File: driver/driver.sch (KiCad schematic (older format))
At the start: 102 parts, among them J1 OUT_A, J10 FAN, J2 OUT_B, J3 UART_DEBUG, J4 USB_B_Micro, J5 CH340E module, J6 1602 I2C LCD, J7 IN_VCC, J8 IN_GND, J9 SWD, Q1 TPHR6503PL, Q2 TPHR6503PL, Q3 TPHR6503PL, Q4 TPHR6503PL, SW2 SW_Push, U1 MT3608, U10 PC817, U2 AMS1117-5.0, U3 AMS1117-3.3, U4 TC4427, U5 TC4427, U6 STM32F103C8Tx, U7 INA226, U8 MCP9804_MSOP, U9 PC817, Y1 8MHz

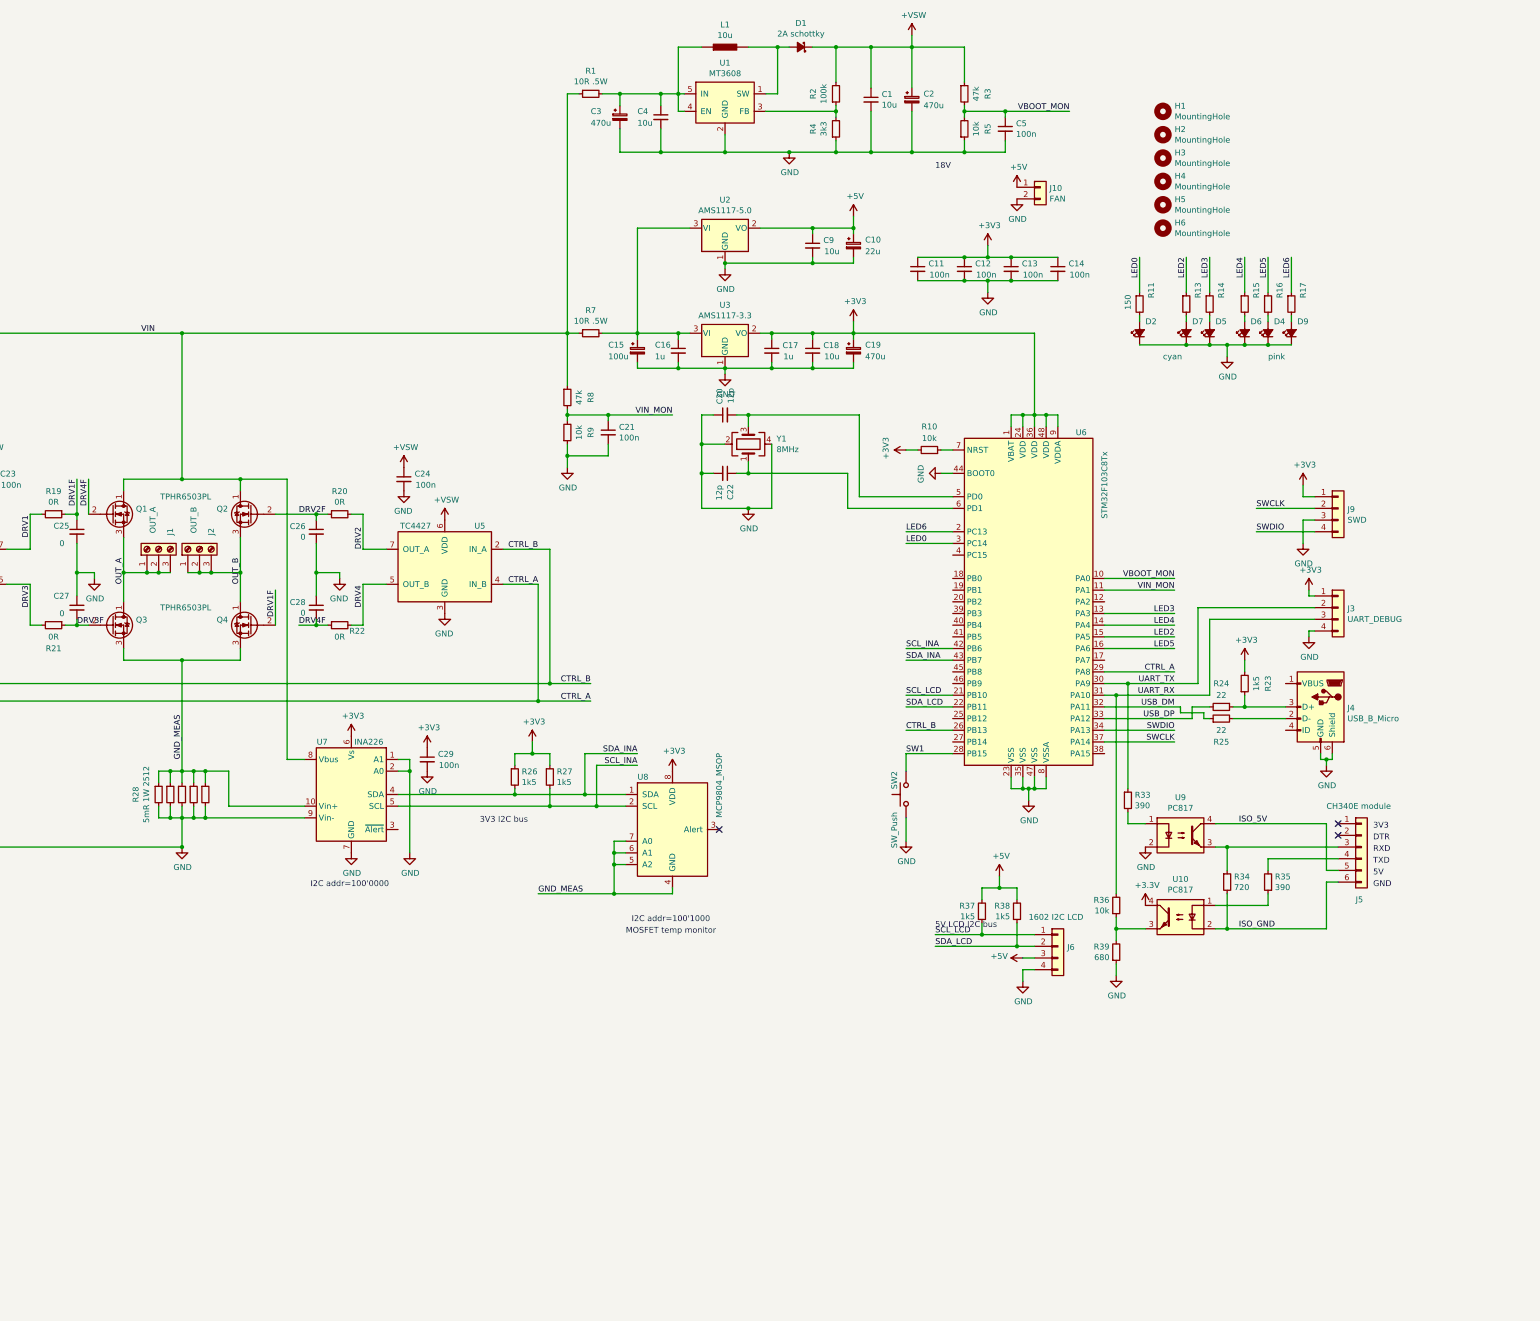
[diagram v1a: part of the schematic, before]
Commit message: Throw out a bunch, use a different microcontroller
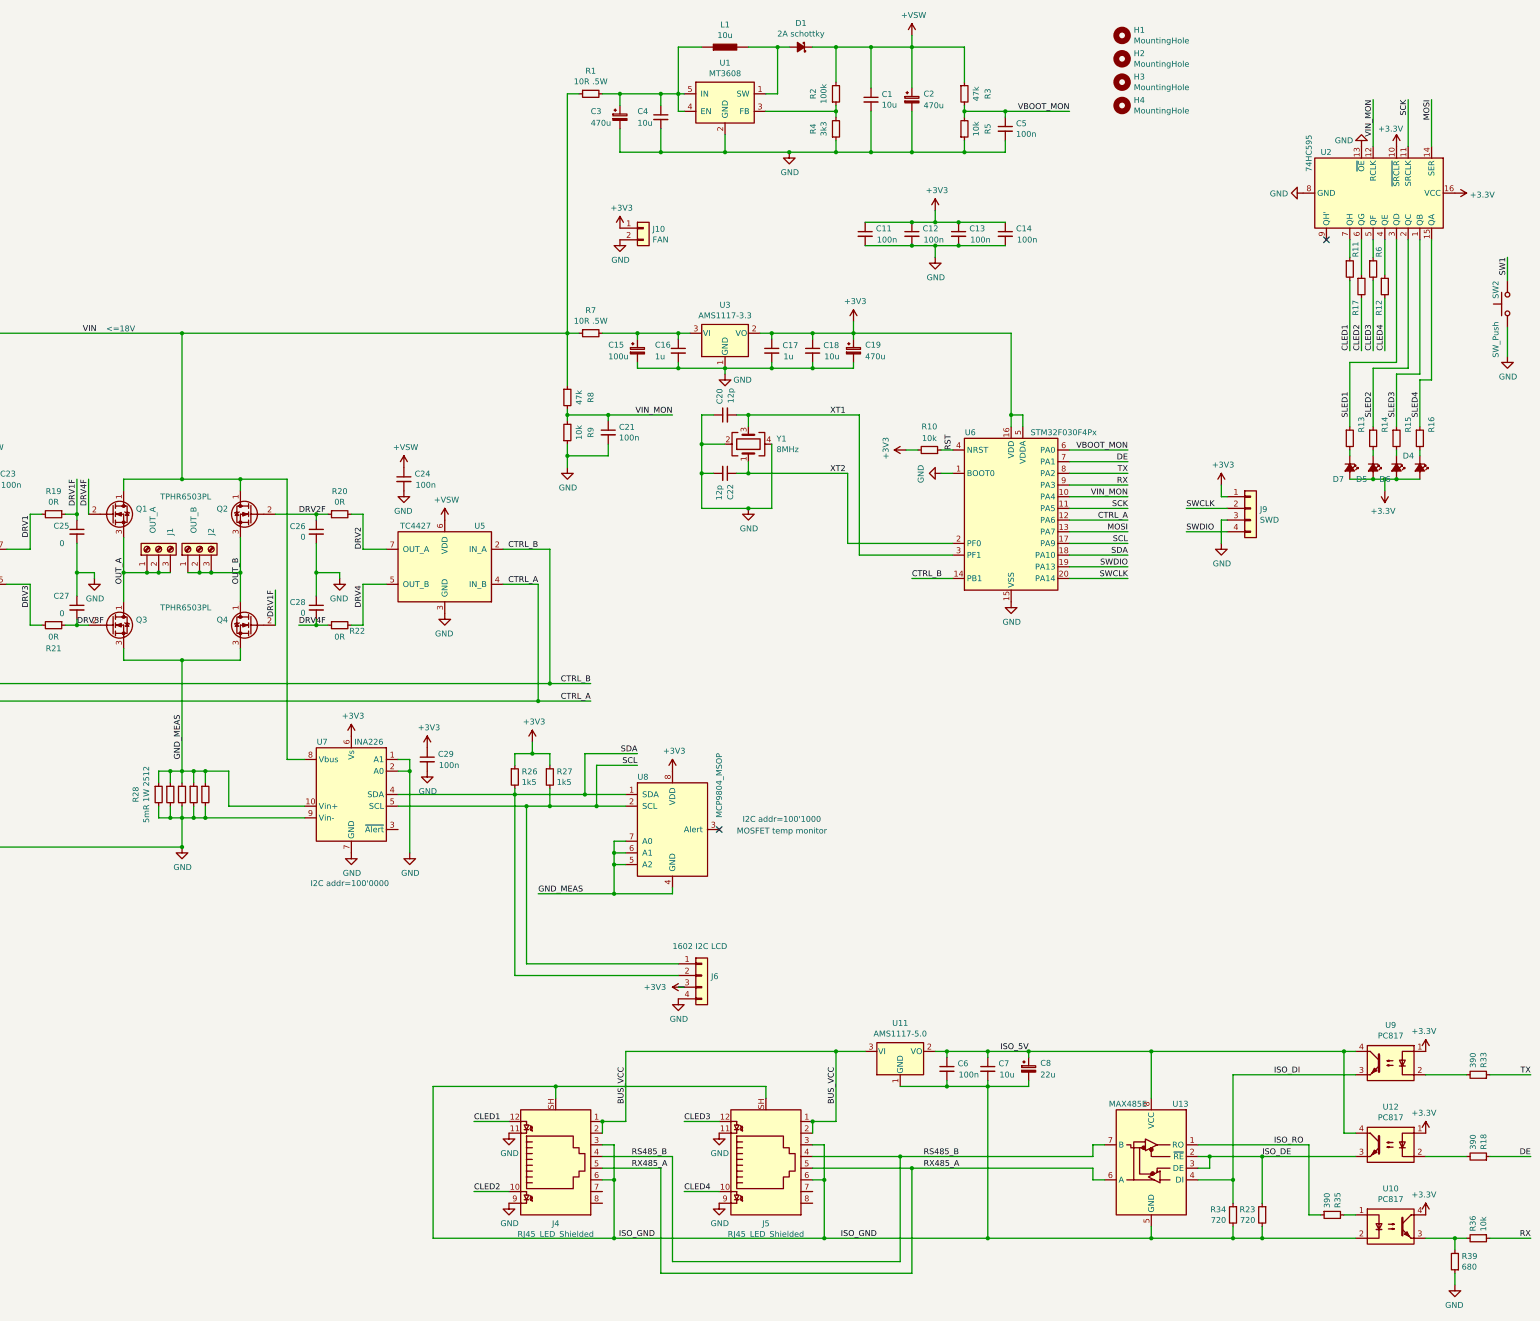
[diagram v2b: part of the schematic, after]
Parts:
- removed C10: 22u, Capacitor_THT:CP_Radial_D5.0mm_P2.00mm, symbol Device:CP_Small
- removed C9: 10u, Capacitors_SMD:C_0603_HandSoldering, symbol Device:C_Small
- removed D2: cyan, LED_SMD:LED_PLCC_2835_Handsoldering, symbol Device:LED_Small_ALT
- removed D9: pink, LED_SMD:LED_PLCC_2835_Handsoldering, symbol Device:LED_Small_ALT
- removed H5, H6: MountingHole, MountingHole:MountingHole_3.2mm_M3, symbol Mechanical:MountingHole
- removed J3: UART_DEBUG, Pin_Headers:Pin_Header_Straight_1x04_Pitch2.54mm, symbol Connector_Generic:Conn_01x04
- removed J4: USB_B_Micro, footprints:microusb_ali_dovetail, symbol Connector:USB_B_Micro
- removed J5: CH340E module, Pin_Headers:Pin_Header_Straight_1x06_Pitch2.54mm, symbol Connector_Generic:Conn_01x06
- removed R24, R25: 22, Resistor_SMD:R_0603_1608Metric_Pad1.05x0.95mm_HandSolder, symbol Device:R_Small
- removed R37, R38: 1k5, Resistor_SMD:R_0603_1608Metric_Pad1.05x0.95mm_HandSolder, symbol Device:R_Small
- removed U2: AMS1117-5.0, Package_TO_SOT_SMD:SOT-223-3_TabPin2, symbol Regulator_Linear:AMS1117-3.3
- removed U6: STM32F103C8Tx, Package_QFP:LQFP-48_7x7mm_P0.5mm, symbol MCU_ST_STM32F1:STM32F103C8Tx
- added C6: 100n, Capacitors_SMD:C_0603_HandSoldering, symbol Device:C_Small
- added C7: 10u, Capacitors_SMD:C_0603_HandSoldering, symbol Device:C_Small
- added C8: 22u, Capacitor_THT:CP_Radial_D5.0mm_P2.00mm, symbol Device:CP_Small
- added J4, J5: RJ45_LED_Shielded, Connector_RJ:RJ45_Amphenol_RJHSE538X, symbol Connector:RJ45_LED_Shielded
- added R12, R6: 150, Resistor_SMD:R_0603_1608Metric_Pad1.05x0.95mm_HandSolder, symbol Device:R_Small
- added R18: 390, Resistor_SMD:R_0603_1608Metric_Pad1.05x0.95mm_HandSolder, symbol Device:R_Small
- added U11: AMS1117-5.0, Package_TO_SOT_SMD:SOT-223-3_TabPin2, symbol Regulator_Linear:AMS1117-3.3
- added U12: PC817, Package_DIP:DIP-4_W7.62mm, symbol Isolator:PC817
- added U13: MAX485E, Package_SO:SO-8_5.3x6.2mm_P1.27mm, symbol Interface_UART:MAX485E
- added U2: 74HC595, Package_SO:SOIC-16_3.9x9.9mm_P1.27mm, symbol 74xx:74HC595
- added U6: STM32F030F4Px, Package_SO:TSSOP-20_4.4x6.5mm_P0.65mm, symbol MCU_ST_STM32F0:STM32F030F4Px
- R23: value 1k5 -> 720
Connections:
- net +5V is gone; now on net +3V3: J10.1 (Pin_1), J6.3 (Pin_3)
- net SCL_LCD is gone; now on net SCL: J6.1 (Pin_1)
- net SDA_LCD is gone; now on net SDA: J6.2 (Pin_2)
- net UART_RX is gone; now on an unnamed net: R36.2
- net +3V3: now also D4.2 (A), D5.2 (A), D6.2 (A), D7.2 (A), U9.1, U12.1, U2.10 (~SRCLR), U2.16 (VCC), U6.16 (VDD), U6.5 (VDDA); no longer R23.2
- net CTRL_A: now also U6.12 (PA6)
- net CTRL_B: now also U6.14 (PB1)
- net GND: now also J4.11, J4.9, J5.11, J5.9, U2.13 (~OE), U2.8 (GND), U6.1 (BOOT0), U6.15 (VSS); no longer D4.1 (K), D5.1 (K), D6.1 (K), D7.1 (K), U9.2
- net ISO_5V: now also C6.1, C7.1, C8.1, U11.2 (VO), U12.4, U13.8 (VCC)
- net ISO_GND: now also R23.2, C6.2, C7.2, C8.2, J4.3, J4.6, J4.SH, J5.3, J5.6, J5.SH, U11.1 (GND), U13.5 (GND)
- net SWCLK: now also U6.20 (PA14)
- net SWDIO: now also U6.19 (PA13)
- net VBOOT_MON: now also U6.6 (PA0)
- net VIN_MON: now also U2.12 (RCLK), U6.10 (PA4)
- net XT1: now reaches C20.2, Y1.3
- net XT1: now also U6.3 (PF1)
- net XT2: now reaches C22.1, Y1.1
- net XT2: now also U6.2 (PF0)
- net RST: now reaches R10.1
- net RST: now also U6.4 (NRST)
- net ISO_DE: now reaches R23.1
- net ISO_DE: now also U12.3, U13.2 (~RE), U13.3 (DE)
- net at U10.1: now also R35.2; no longer R35.1
- net at R39.2, U10.3: no longer R36.1
- net at R33.2: now also U9.2; no longer U9.1
- net ISO_DI: now reaches R34.1, U9.3
- net ISO_DI: now also U13.4 (DI)
- net CLED1: now reaches R11.2
- net CLED1: now also J4.12
- net at R16.2: now also D4.1 (K); no longer D4.2 (A)
- net at R14.2: now also D5.1 (K); no longer D5.2 (A)
- net at R15.2: now also D6.1 (K); no longer D6.2 (A)
- net at R13.2: now also D7.1 (K); no longer D7.2 (A)
- net CLED2: now reaches R17.2
- net CLED2: now also J4.10
- net LED0: no longer names the net of R11.1
- net LED0: now also U2.7 (QH)
- net LED2 renamed SLED1
- net SLED1: now also U2.3 (QD)
- net LED3 renamed SLED2
- net SLED2: now also U2.2 (QC)
- net LED4 renamed SLED3
- net SLED3: now also U2.1 (QB)
- net LED5 renamed SLED4
- net SLED4: now also U2.15 (QA)
- net LED6: no longer names the net of R17.1
- net LED6: now also U2.6 (QG)
- net SCL_INA renamed SCL
- net SCL: now also U6.17 (PA9)
- net SDA_INA renamed SDA
- net SDA: now also U6.18 (PA10)
- net UART_TX renamed TX
- net TX: now also U6.8 (PA2)
- new net: R18.2, U12.2
- new net: R12.1, U2.4 (QE)
- new net: R6.1, U2.5 (QF)
- new net BUS_VCC: J4.1, J4.2, J5.1, J5.2, U11.3 (VI)
- new net CLED3: J5.12, R6.2
- new net CLED4: J5.10, R12.2
- new net DE: R18.1, U6.7 (PA1)
- new net ISO_RO: R35.1, U13.1 (RO)
- new net MOSI: U2.14 (SER), U6.13 (PA7)
- new net RS485_B: J4.4, J5.4, U13.7 (B)
- new net RX: R36.1, U6.9 (PA3)
- new net RX485_A: J4.5, J5.5, U13.6 (A)
- new net SCK: U2.11 (SRCLK), U6.11 (PA5)
- no-connect marks 3 -> 2
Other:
- note added: "<=18V"
- note removed: "18V"
- note removed: "3V3"
- note removed: "3V3 I2C bus"
- note removed: "5V"
- note removed: "5V LCD I2C bus"
- note removed: "DTR"
- note removed: "GND"
- note removed: "RXD"
- note removed: "TXD"
- moved on the sheet: C11, C12, C13, C14, D4, D5, D6, D7, H1, H2, H3, H4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

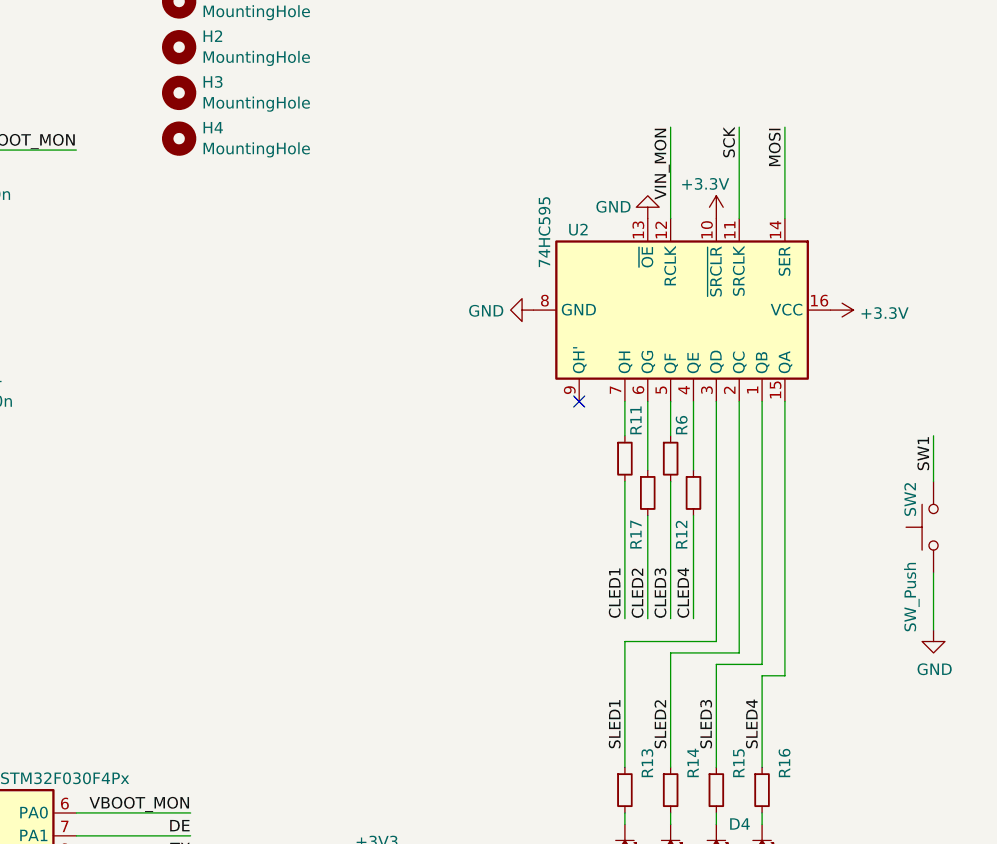
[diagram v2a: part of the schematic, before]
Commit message: driver: Add mounting holes for heatsink
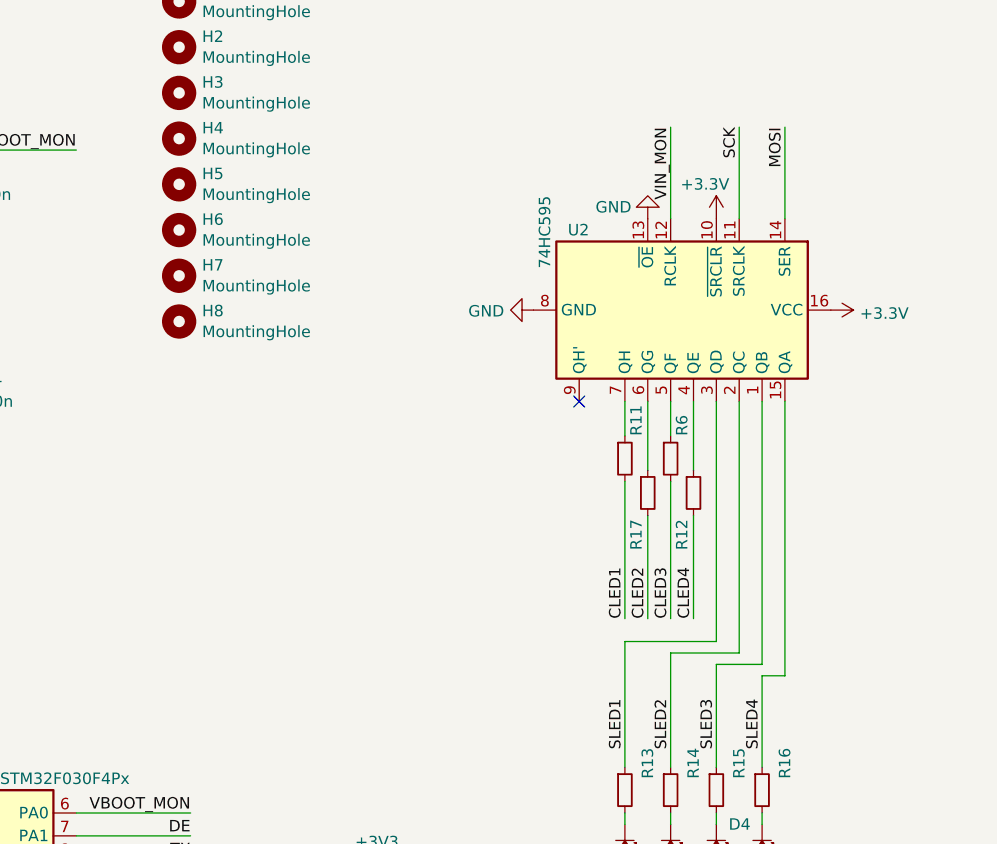
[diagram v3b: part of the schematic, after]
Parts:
- removed SW2: SW_Push, Button_Switch_THT:SW_PUSH_6mm, symbol Switch:SW_Push
- added H5, H6, H7, H8: MountingHole, MountingHole:MountingHole_3.2mm_M3, symbol Mechanical:MountingHole
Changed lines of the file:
@@
 SLED4
-$Comp
-L Switch:SW_Push SW2
-U 1 1 5D6024EE
-P 20700 3850
-F 0 "SW2" H 20900 3950 50  0000 R CNN
-F 1 "SW_Push" H 20550 3950 50  0000 R CNN
-F 2 "Button_Switch_THT:SW_PUSH_6mm" H 20700 4050 50  0001 C CNN
-F 3 "" H 20700 4050 50  0001 C CNN
-	1    20700 3850
-	0    -1   -1   0
-$EndComp
-$Comp
-L power:GND #PWR0143
-U 1 1 5D60402D
-P 20700 4300
-F 0 "#PWR0143" H 20700 4050 50  0001 C CNN
-F 1 "GND" H 20705 4127 50  0000 C CNN
-F 2 "" H 20700 4300 50  0001 C CNN
-F 3 "" H 20700 4300 50  0001 C CNN
-	1    20700 4300
-	1    0    0    -1
-$EndComp
-Wire Wire Line
-	20700 4300 20700 4050
-Wire Wire Line
-	20700 3450 20700 3650
-Text Label 20700 3450 3    50   ~ 0
-SW1
 $Comp
 L Sensor_Temperature:MCP9804_MSOP U8
@@
 Wire Wire Line
 	16250 11850 14850 11850
+$Comp
+L Mechanical:MountingHole H5
+U 1 1 5C580F0A
+P 17400 2350
+F 0 "H5" H 17500 2396 50  0000 L CNN
+F 1 "MountingHole" H 17500 2305 50  0000 L CNN
+F 2 "MountingHole:MountingHole_3.2mm_M3" H 17400 2350 50  0001 C CNN
+F 3 "~" H 17400 2350 50  0001 C CNN
+	1    17400 2350
+	1    0    0    -1
+$EndComp
+$Comp
+L Mechanical:MountingHole H6
+U 1 1 5C580F10
+P 17400 2550
+F 0 "H6" H 17500 2596 50  0000 L CNN
+F 1 "MountingHole" H 17500 2505 50  0000 L CNN
+F 2 "MountingHole:MountingHole_3.2mm_M3" H 17400 2550 50  0001 C CNN
+F 3 "~" H 17400 2550 50  0001 C CNN
+	1    17400 2550
+	1    0    0    -1
+$EndComp
+$Comp
+L Mechanical:MountingHole H7
+U 1 1 5C580F16
+P 17400 2750
+F 0 "H7" H 17500 2796 50  0000 L CNN
+F 1 "MountingHole" H 17500 2705 50  0000 L CNN
+F 2 "MountingHole:MountingHole_3.2mm_M3" H 17400 2750 50  0001 C CNN
+F 3 "~" H 17400 2750 50  0001 C CNN
+	1    17400 2750
+	1    0    0    -1
+$EndComp
+$Comp
+L Mechanical:MountingHole H8
+U 1 1 5C580F1C
+P 17400 2950
+F 0 "H8" H 17500 2996 50  0000 L CNN
+F 1 "MountingHole" H 17500 2905 50  0000 L CNN
+F 2 "MountingHole:MountingHole_3.2mm_M3" H 17400 2950 50  0001 C CNN
+F 3 "~" H 17400 2950 50  0001 C CNN
+	1    17400 2950
+	1    0    0    -1
+$EndComp
 $EndSCHEMATC
